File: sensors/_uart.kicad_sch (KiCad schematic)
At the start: 22 parts, among them J5 JP_GPS, J6 JP_RADIO, U1 SC16IS752IPW, Y1 14.7456MHz

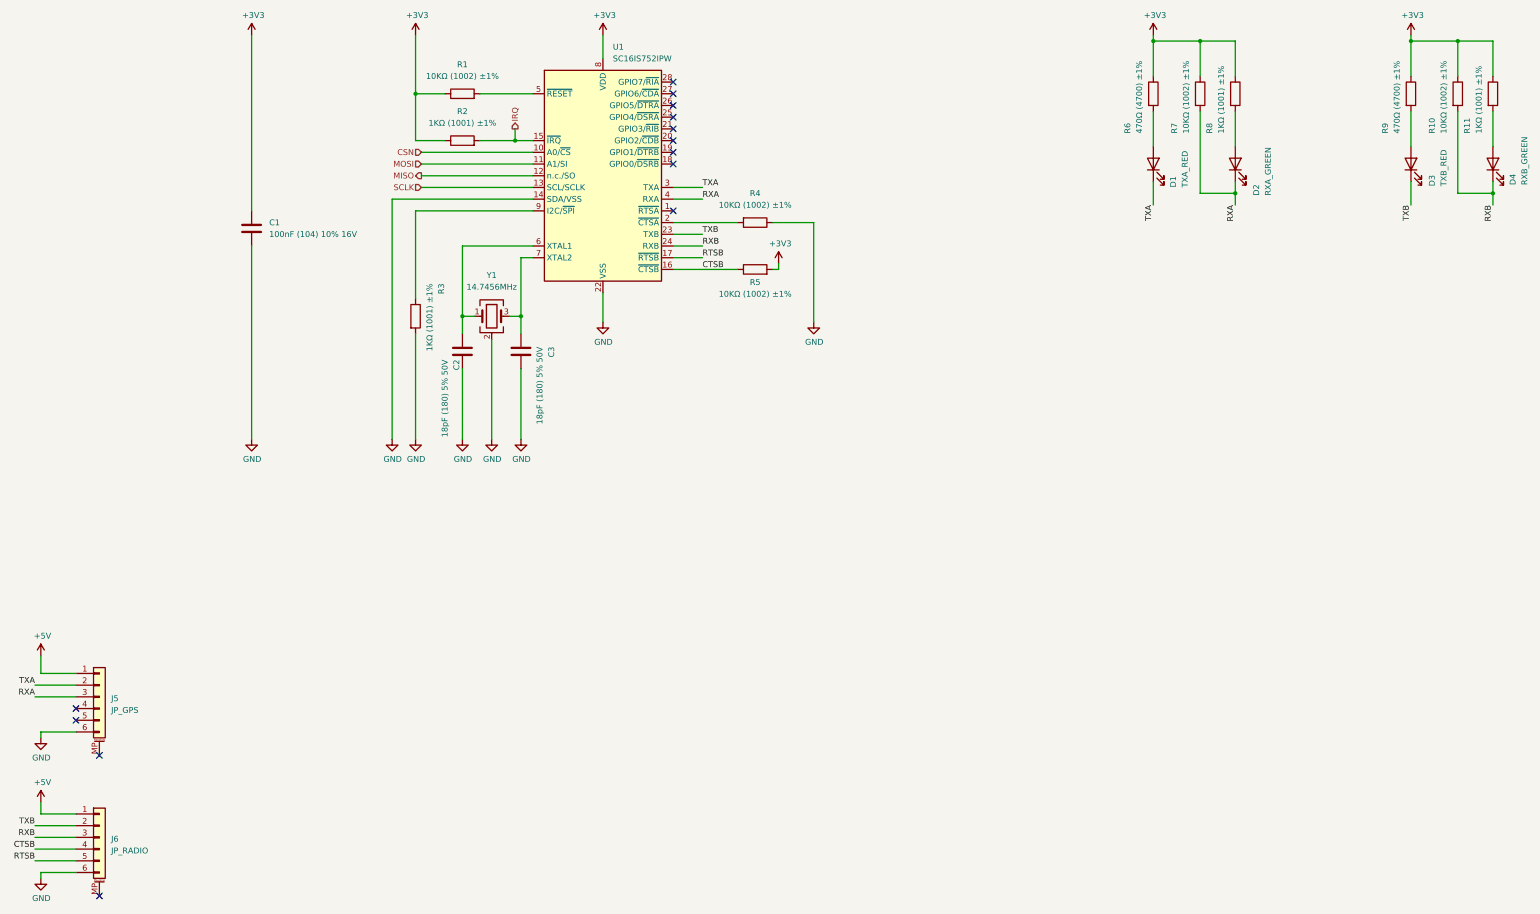
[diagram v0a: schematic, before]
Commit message: add IMU
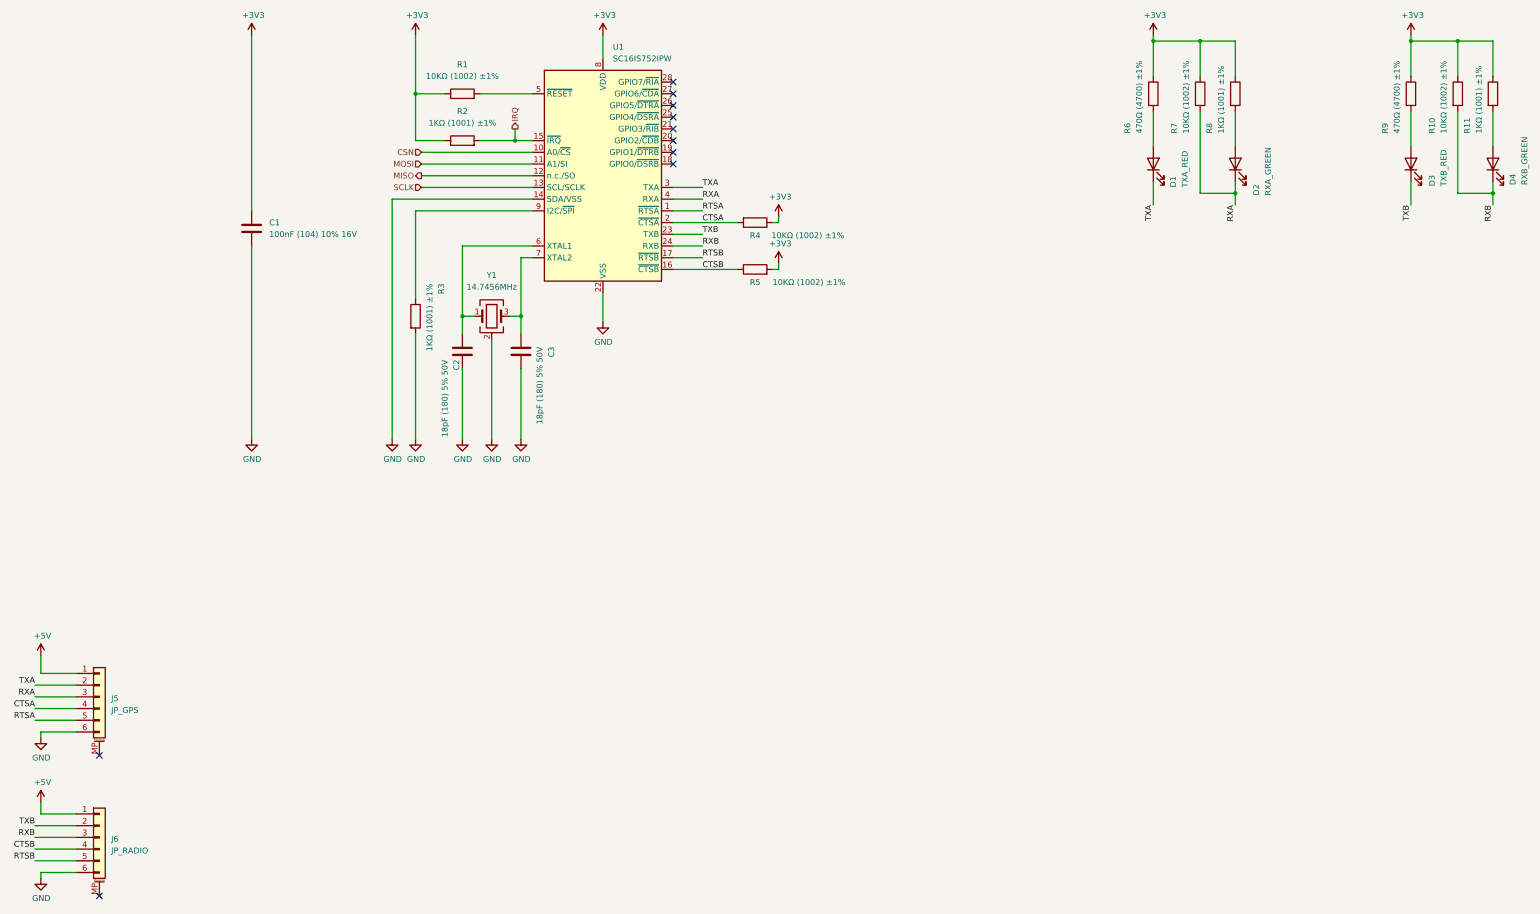
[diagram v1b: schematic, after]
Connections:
- net +3V3: now also R4.1
- net GND: no longer R4.1
- net CTSA: now reaches R4.2, U1.2 (~{CTSA})
- net CTSA: now also J5.4 (Pin_4)
- net RTSA: now reaches J5.5 (Pin_5)
- net RTSA: now also U1.1 (~{RTSA})
- no-connect marks 13 -> 10
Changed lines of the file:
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@@
 	)
 	(no_connect
-		(at 167.64 106.68)
-	)
-	(no_connect
 		(at 167.64 91.44)
 	)
 	(no_connect
-		(at 38.1 217.17)
-	)
-	(no_connect
 		(at 167.64 78.74)
 	)
@@
 		(at 167.64 96.52)
 	)
-	(no_connect
-		(at 38.1 214.63)
-	)
 	(wire
 		(pts
@@
 	(wire
 		(pts
+			(xy 29.21 217.17) (xy 38.1 217.17)
+		)
+		(stroke
+			(width 0)
+			(type default)
+		)
+	)
+	(wire
+		(pts
 			(xy 133.35 88.9) (xy 133.35 91.44)
 		)
@@
 	(wire
 		(pts
+			(xy 190.5 109.22) (xy 190.5 107.95)
+		)
+		(stroke
+			(width 0)
+			(type default)
+		)
+	)
+	(wire
+		(pts
 			(xy 121.92 129.54) (xy 124.46 129.54)
 		)
@@
 	(wire
 		(pts
+			(xy 167.64 106.68) (xy 173.99 106.68)
+		)
+		(stroke
+			(width 0)
+			(type default)
+		)
+	)
+	(wire
+		(pts
 			(xy 152.4 68.58) (xy 152.4 73.66)
 		)
@@
 	(wire
 		(pts
-			(xy 29.21 240.03) (xy 38.1 240.03)
+			(xy 189.23 109.22) (xy 190.5 109.22)
 		)
 		(stroke
@@
 	(wire
 		(pts
-			(xy 121.92 140.97) (xy 121.92 156.21)
+			(xy 29.21 240.03) (xy 38.1 240.03)
 		)
 		(stroke
@@
 	(wire
 		(pts
-			(xy 345.44 77.47) (xy 345.44 69.85)
+			(xy 121.92 140.97) (xy 121.92 156.21)
 		)
 		(stroke
@@
 	(wire
 		(pts
-			(xy 327.66 69.85) (xy 327.66 77.47)
+			(xy 345.44 77.47) (xy 345.44 69.85)
 		)
 		(stroke
@@
 	(wire
 		(pts
-			(xy 137.16 114.3) (xy 121.92 114.3)
+			(xy 327.66 69.85) (xy 327.66 77.47)
 		)
 		(stroke
@@
 	(wire
 		(pts
-			(xy 345.44 100.33) (xy 345.44 102.87)
+			(xy 137.16 114.3) (xy 121.92 114.3)
 		)
 		(stroke
@@
 	(wire
 		(pts
-			(xy 29.21 245.11) (xy 38.1 245.11)
+			(xy 345.44 100.33) (xy 345.44 102.87)
 		)
 		(stroke
@@
 	(wire
 		(pts
-			(xy 198.12 109.22) (xy 198.12 130.81)
+			(xy 29.21 245.11) (xy 38.1 245.11)
 		)
 		(stroke
@@
 	(wire
 		(pts
-			(xy 189.23 109.22) (xy 198.12 109.22)
+			(xy 29.21 214.63) (xy 38.1 214.63)
 		)
 		(stroke
@@
 		)
 	)
+	(label "CTSA"
+		(at 173.99 109.22 0)
+		(effects
+			(font
+				(size 1.27 1.27)
+			)
+			(justify left bottom)
+		)
+	)
+	(label "CTSA"
+		(at 29.21 214.63 180)
+		(effects
+			(font
+				(size 1.27 1.27)
+			)
+			(justify right bottom)
+		)
+	)
 	(label "TXB"
 		(at 173.99 111.76 0)
@@
 		)
 	)
+	(label "RTSA"
+		(at 29.21 217.17 180)
+		(effects
+			(font
+				(size 1.27 1.27)
+			)
+			(justify right bottom)
+		)
+	)
 	(label "RXB"
 		(at 345.44 105.41 270)
@@
 		)
 	)
+	(label "RTSA"
+		(at 173.99 106.68 0)
+		(effects
+			(font
+				(size 1.27 1.27)
+			)
+			(justify left bottom)
+		)
+	)
 	(label "RXA"
 		(at 29.21 212.09 180)
@@
 		(in_pos_files yes)
 		(dnp no)
-		(fields_autoplaced yes)
 		(property "Reference" "R4"
-			(at 185.42 102.87 90)
+			(at 185.42 112.014 90)
 			(show_name no)
 			(do_not_autoplace no)
@@
 		)
 		(property "Value" "10KΩ (1002) ±1%"
-			(at 185.42 105.41 90)
+			(at 196.85 112.014 90)
 			(show_name no)
 			(do_not_autoplace no)
@@
 	(symbol
 		(lib_id "power:GND")
-		(at 198.12 130.81 0)
-		(unit 1)
-		(body_style 1)
-		(exclude_from_sim no)
-		(in_bom yes)
-		(on_board yes)
-		(in_pos_files yes)
-		(dnp no)
-		(property "Reference" "#PWR025"
-			(at 198.12 137.16 0)
-			(hide yes)
-			(show_name no)
-			(do_not_autoplace no)
-			(effects
-				(font
-					(size 1.27 1.27)
-				)
-			)
-		)
-		(property "Value" "GND"
-			(at 198.2343 135.1344 0)
-			(show_name no)
-			(do_not_autoplace no)
-			(effects
-				(font
-					(size 1.27 1.27)
-				)
-			)
-		)
-		(property "Footprint" ""
-			(at 198.12 130.81 0)
-			(show_name no)
-			(do_not_autoplace no)
-			(effects
-				(font
-					(size 1.27 1.27)
-				)
-			)
-		)
-		(property "Datasheet" ""
-			(at 198.12 130.81 0)
-			(show_name no)
-			(do_not_autoplace no)
-			(effects
-				(font
-					(size 1.27 1.27)
-				)
-			)
-		)
-		(property "Description" "Power symbol creates a global label with name \"GND\" , ground"
-			(at 198.12 130.81 0)
-			(hide yes)
-			(show_name no)
-			(do_not_autoplace no)
-			(effects
-				(font
-					(size 1.27 1.27)
-				)
-			)
-		)
-		(pin "1"
-		)
-		(instances
-			(project "sensors"
-				(path "/e63e39d7-6ac0-4ffd-8aa3-1841a4541b55/243469ce-cfff-4f38-a791-94cacfa4b28b"
-					(reference "#PWR025")
-					(unit 1)
-				)
-			)
-		)
-	)
-	(symbol
-		(lib_id "power:GND")
 		(at 128.27 156.21 0)
 		(unit 1)
@@
 	(symbol
 		(lib_id "power:+3.3V")
+		(at 190.5 107.95 0)
+		(unit 1)
+		(body_style 1)
+		(exclude_from_sim no)
+		(in_bom yes)
+		(on_board yes)
+		(in_pos_files yes)
+		(dnp no)
+		(property "Reference" "#PWR030"
+			(at 190.5 111.76 0)
+			(hide yes)
+			(show_name no)
+			(do_not_autoplace no)
+			(effects
+				(font
+					(size 1.27 1.27)
+				)
+			)
+		)
+		(property "Value" "+3V3"
+			(at 190.8683 103.6256 0)
+			(show_name no)
+			(do_not_autoplace no)
+			(effects
+				(font
+					(size 1.27 1.27)
+				)
+			)
+		)
+		(property "Footprint" ""
+			(at 190.5 107.95 0)
+			(show_name no)
+			(do_not_autoplace no)
+			(effects
+				(font
+					(size 1.27 1.27)
+				)
+			)
+		)
+		(property "Datasheet" ""
+			(at 190.5 107.95 0)
+			(show_name no)
+			(do_not_autoplace no)
+			(effects
+				(font
+					(size 1.27 1.27)
+				)
+			)
+		)
+		(property "Description" "Power symbol creates a global label with name \"+3.3V\""
+			(at 190.5 107.95 0)
+			(hide yes)
+			(show_name no)
+			(do_not_autoplace no)
+			(effects
+				(font
+					(size 1.27 1.27)
+				)
+			)
+		)
+		(pin "1"
+		)
+		(instances
+			(project "sensors"
+				(path "/e63e39d7-6ac0-4ffd-8aa3-1841a4541b55/243469ce-cfff-4f38-a791-94cacfa4b28b"
+					(reference "#PWR030")
+					(unit 1)
+				)
+			)
+		)
+	)
+	(symbol
+		(lib_id "power:+3.3V")
 		(at 76.2 68.58 0)
 		(unit 1)
@@
 		)
 		(property "Value" "10KΩ (1002) ±1%"
-			(at 185.42 124.714 90)
+			(at 197.104 122.174 90)
 			(show_name no)
 			(do_not_autoplace no)

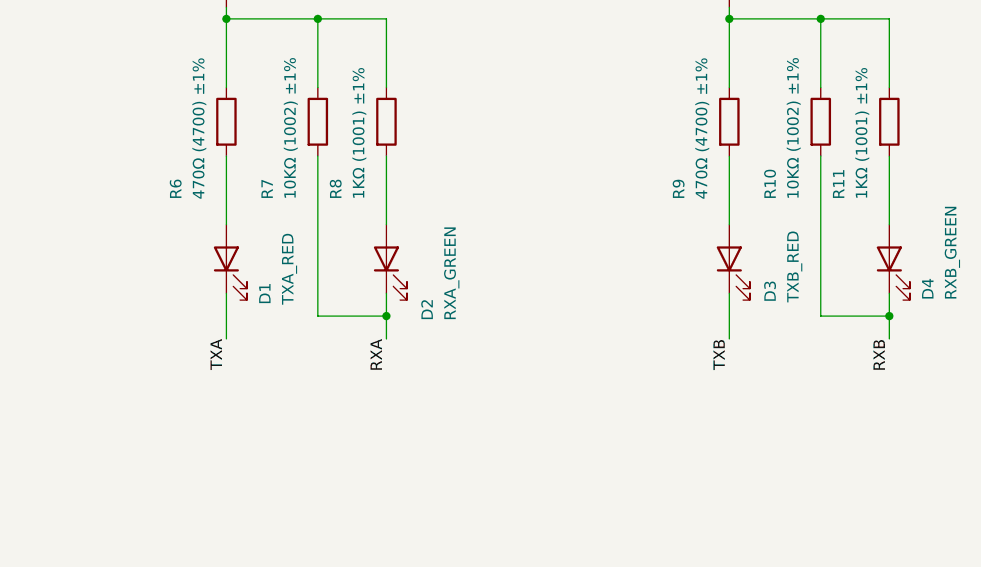
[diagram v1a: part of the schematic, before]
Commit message: switch RED/GREEN LEDs
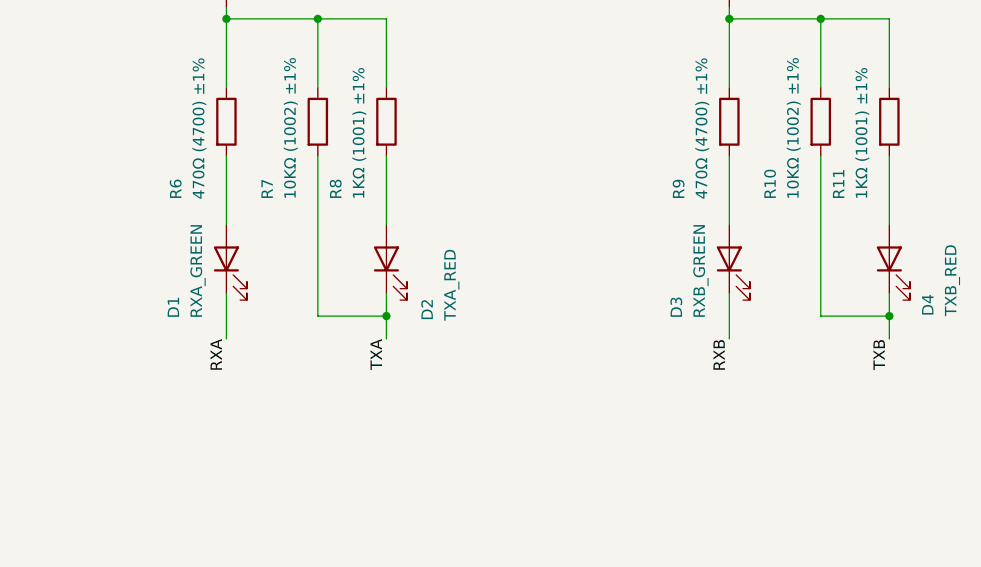
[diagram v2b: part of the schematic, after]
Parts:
- D1: value TXA_RED -> RXA_GREEN
- D2: value RXA_GREEN -> TXA_RED
- D3: value TXB_RED -> RXB_GREEN
- D4: value RXB_GREEN -> TXB_RED
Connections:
- net RXA: now also D1.1 (K); no longer D2.1 (K), R7.2
- net RXB: now also D3.1 (K); no longer D4.1 (K), R10.2
- net TXA: now also D2.1 (K), R7.2; no longer D1.1 (K)
- net TXB: now also D4.1 (K), R10.2; no longer D3.1 (K)
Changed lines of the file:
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@@
 	)
 	(label "RXA"
-		(at 289.56 105.41 270)
+		(at 271.78 105.41 270)
 		(effects
 			(font
@@
 	)
 	(label "RXB"
-		(at 345.44 105.41 270)
+		(at 327.66 105.41 270)
 		(effects
 			(font
@@
 	)
 	(label "TXB"
-		(at 327.66 105.41 270)
+		(at 345.44 105.41 270)
 		(effects
 			(font
@@
 	)
 	(label "TXA"
-		(at 271.78 105.41 270)
+		(at 289.56 105.41 270)
 		(effects
 			(font
@@
 		(dnp no)
 		(property "Reference" "D3"
-			(at 332.232 101.346 0)
+			(at 321.818 103.124 0)
 			(show_name no)
 			(do_not_autoplace no)
@@
 			)
 		)
-		(property "Value" "TXB_RED"
-			(at 334.772 101.346 0)
+		(property "Value" "RXB_GREEN"
+			(at 324.358 103.124 0)
 			(show_name no)
 			(do_not_autoplace no)
@@
 		(dnp no)
 		(property "Reference" "D1"
-			(at 276.098 101.6 0)
+			(at 265.938 103.124 0)
 			(show_name no)
 			(do_not_autoplace no)
@@
 			)
 		)
-		(property "Value" "TXA_RED"
-			(at 278.638 101.6 0)
+		(property "Value" "RXA_GREEN"
+			(at 268.478 103.124 0)
 			(show_name no)
 			(do_not_autoplace no)
@@
 		(dnp no)
 		(property "Reference" "D4"
-			(at 349.758 101.092 0)
+			(at 349.758 102.87 0)
 			(show_name no)
 			(do_not_autoplace no)
@@
 			)
 		)
-		(property "Value" "RXB_GREEN"
-			(at 352.298 101.092 0)
+		(property "Value" "TXB_RED"
+			(at 352.298 102.87 0)
 			(show_name no)
 			(do_not_autoplace no)
@@
 			)
 		)
-		(property "Value" "RXA_GREEN"
+		(property "Value" "TXA_RED"
 			(at 296.672 103.378 0)
 			(show_name no)

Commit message: routing
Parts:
- D1: value RXA_GREEN -> TXA_RED
- D2: value TXA_RED -> RXA_GREEN
- D3: value RXB_GREEN -> TXB_RED
- D4: value TXB_RED -> RXB_GREEN
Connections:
- net RXA: now also D2.1 (K), R7.2; no longer D1.1 (K)
- net RXB: now also D4.1 (K), R10.2; no longer D3.1 (K)
- net TXA: now also D1.1 (K); no longer D2.1 (K), R7.2
- net TXB: now also D3.1 (K); no longer D4.1 (K), R10.2
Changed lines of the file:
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@@
 	)
 	(label "RXA"
-		(at 271.78 105.41 270)
+		(at 289.56 105.41 270)
 		(effects
 			(font
@@
 	)
 	(label "RXB"
-		(at 327.66 105.41 270)
+		(at 345.44 105.41 270)
 		(effects
 			(font
@@
 	)
 	(label "TXB"
-		(at 345.44 105.41 270)
+		(at 327.66 105.41 270)
 		(effects
 			(font
@@
 	)
 	(label "TXA"
-		(at 289.56 105.41 270)
+		(at 271.78 105.41 270)
 		(effects
 			(font
@@
 		(dnp no)
 		(property "Reference" "D3"
-			(at 321.818 103.124 0)
+			(at 321.818 101.346 0)
 			(show_name no)
 			(do_not_autoplace no)
@@
 			)
 		)
-		(property "Value" "RXB_GREEN"
-			(at 324.358 103.124 0)
+		(property "Value" "TXB_RED"
+			(at 324.358 101.346 0)
 			(show_name no)
 			(do_not_autoplace no)
@@
 		(dnp no)
 		(property "Reference" "D1"
-			(at 265.938 103.124 0)
+			(at 265.938 101.6 0)
 			(show_name no)
 			(do_not_autoplace no)
@@
 			)
 		)
-		(property "Value" "RXA_GREEN"
-			(at 268.478 103.124 0)
+		(property "Value" "TXA_RED"
+			(at 268.478 101.6 0)
 			(show_name no)
 			(do_not_autoplace no)
@@
 		(dnp no)
 		(property "Reference" "D4"
-			(at 349.758 102.87 0)
+			(at 349.758 101.092 0)
 			(show_name no)
 			(do_not_autoplace no)
@@
 			)
 		)
-		(property "Value" "TXB_RED"
-			(at 352.298 102.87 0)
+		(property "Value" "RXB_GREEN"
+			(at 352.298 101.092 0)
 			(show_name no)
 			(do_not_autoplace no)
@@
 		(dnp no)
 		(property "Reference" "D2"
-			(at 294.132 103.378 0)
+			(at 294.132 101.6 0)
 			(show_name no)
 			(do_not_autoplace no)
@@
 			)
 		)
-		(property "Value" "TXA_RED"
-			(at 296.672 103.378 0)
-			(show_name no)
-			(do_not_autoplace no)
+		(property "Value" "RXA_GREEN"
+			(at 296.672 101.6 0)
+			(show_name no)
+			(do_not_autoplace no)

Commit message: move buzzer to power board
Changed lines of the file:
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@@
+	(wire
+		(pts
+			(xy 128.27 121.92) (xy 128.27 124.46)
+		)
+		(stroke
+			(width 0)
+			(type default)
+		)
+	)
 	(wire
 		(pts
@@
 	)
 	(symbol
+		(lib_id "power:GND")
+		(at 128.27 121.92 180)
+		(unit 1)
+		(body_style 1)
+		(exclude_from_sim no)
+		(in_bom yes)
+		(on_board yes)
+		(in_pos_files yes)
+		(dnp no)
+		(property "Reference" "#PWR063"
+			(at 128.27 115.57 0)
+			(hide yes)
+			(show_name no)
+			(do_not_autoplace no)
+			(effects
+				(font
+					(size 1.27 1.27)
+				)
+			)
+		)
+		(property "Value" "GND"
+			(at 128.1557 117.5956 0)
+			(show_name no)
+			(do_not_autoplace no)
+			(effects
+				(font
+					(size 1.27 1.27)
+				)
+			)
+		)
+		(property "Footprint" ""
+			(at 128.27 121.92 0)
+			(show_name no)
+			(do_not_autoplace no)
+			(effects
+				(font
+					(size 1.27 1.27)
+				)
+			)
+		)
+		(property "Datasheet" ""
+			(at 128.27 121.92 0)
+			(show_name no)
+			(do_not_autoplace no)
+			(effects
+				(font
+					(size 1.27 1.27)
+				)
+			)
+		)
+		(property "Description" "Power symbol creates a global label with name \"GND\" , ground"
+			(at 128.27 121.92 0)
+			(hide yes)
+			(show_name no)
+			(do_not_autoplace no)
+			(effects
+				(font
+					(size 1.27 1.27)
+				)
+			)
+		)
+		(pin "1"
+		)
+		(instances
+			(project "sensors"
+				(path "/e63e39d7-6ac0-4ffd-8aa3-1841a4541b55/243469ce-cfff-4f38-a791-94cacfa4b28b"
+					(reference "#PWR063")
+					(unit 1)
+				)
+			)
+		)
+	)
+	(symbol
 		(lib_id "Device:R")
 		(at 337.82 81.28 0)
@@
 		(fields_autoplaced yes)
 		(property "Reference" "Y1"
-			(at 128.27 120.65 0)
+			(at 137.3921 123.2934 0)
 			(show_name no)
 			(do_not_autoplace no)
@@
 		)
 		(property "Value" "14.7456MHz"
-			(at 128.27 123.19 0)
-			(show_name no)
-			(do_not_autoplace no)
+			(at 137.3921 125.7177 0)
+			(show_name no)
+			(do_not_autoplace no)

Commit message: added JP_VOLTS, Vref select jumper; VBAT_ADC Jumper
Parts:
- C1: Part (none) -> CC0402X7R50V104KN
- D1, D3: Part (none) -> KT-0603R
- D2, D4: Part (none) -> KT-0603G
- R11, R2, R3, R8: Part C25744 -> SCR0402F1K
- Y1: symbol Device:Crystal_GND24 -> pilotpi:Crystal_GND24
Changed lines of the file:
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@@
 			)
 		)
-		(property "Part" "C25744"
+		(property "Part" "SCR0402F1K"
 			(at 121.92 91.44 0)
 			(hide yes)
@@
 			)
 		)
-		(property "Part" ""
+		(property "Part" "KT-0603R"
 			(at 327.66 96.52 0)
 			(hide yes)
@@
 			)
 		)
-		(property "Part" "C25744"
+		(property "Part" "SCR0402F1K"
 			(at 111.76 129.54 0)
 			(hide yes)
@@
 			)
 		)
-		(property "Part" ""
+		(property "Part" "CC0402X7R50V104KN"
 			(at 76.2 110.49 0)
 			(hide yes)
@@
 			)
 		)
-		(property "Part" "C25744"
+		(property "Part" "SCR0402F1K"
 			(at 345.44 81.28 0)
 			(hide yes)
@@
 			)
 		)
-		(property "Part" ""
+		(property "Part" "KT-0603R"
 			(at 271.78 96.52 0)
 			(hide yes)
@@
 			)
 		)
-		(property "Part" "C25744"
+		(property "Part" "SCR0402F1K"
 			(at 289.56 81.28 0)
 			(hide yes)
@@
 	)
 	(symbol
-		(lib_id "Device:Crystal_GND24")
+		(lib_id "pilotpi:Crystal_GND24")
 		(at 128.27 129.54 0)
 		(unit 1)
@@
 		(in_pos_files yes)
 		(dnp no)
-		(fields_autoplaced yes)
 		(property "Reference" "Y1"
-			(at 137.3921 123.2934 0)
+			(at 136.652 127 0)
 			(show_name no)
 			(do_not_autoplace no)
@@
 		)
 		(property "Value" "14.7456MHz"
-			(at 137.3921 125.7177 0)
+			(at 141.478 129.4243 0)
 			(show_name no)
 			(do_not_autoplace no)
@@
 			)
 		)
-		(property "Part" ""
+		(property "Part" "KT-0603G"
 			(at 345.44 96.52 0)
 			(hide yes)
@@
 			)
 		)
-		(property "Part" ""
+		(property "Part" "KT-0603G"
 			(at 289.56 96.52 0)
 			(hide yes)

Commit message: use CLK out from CAN controller for UART (use 16 MHz instead of 14.7456MHz); minor changes
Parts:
- removed C2, C3: 18pF (180) 5% 50V, Capacitor_SMD:C_0402_1005Metric, symbol Device:C
- removed Y1: 14.7456MHz, Crystal:Crystal_SMD_3225-4Pin_3.2x2.5mm, symbol pilotpi:Crystal_GND24
- C1: value 100nF (104) 10% 16V -> 100nF 10% 16V
- R1, R10, R4, R5, R7: value 10KΩ (1002) ±1% -> 10KΩ ±1%
- R11, R2, R3, R8: value 1KΩ (1001) ±1% -> 1KΩ ±1%
- R6, R9: value 470Ω (4700) ±1% -> 470Ω ±1%
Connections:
- net EXTCLK: now reaches U1.6 (XTAL1)
- no-connect marks 10 -> 11
